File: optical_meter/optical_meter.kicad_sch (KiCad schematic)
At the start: 47 parts, among them J1 Conn_02x04, J2 SFP+, J3 Conn_01x02_Pin, U2 FIN1002M5X, U3 FIN1001M5X, U5 Pico

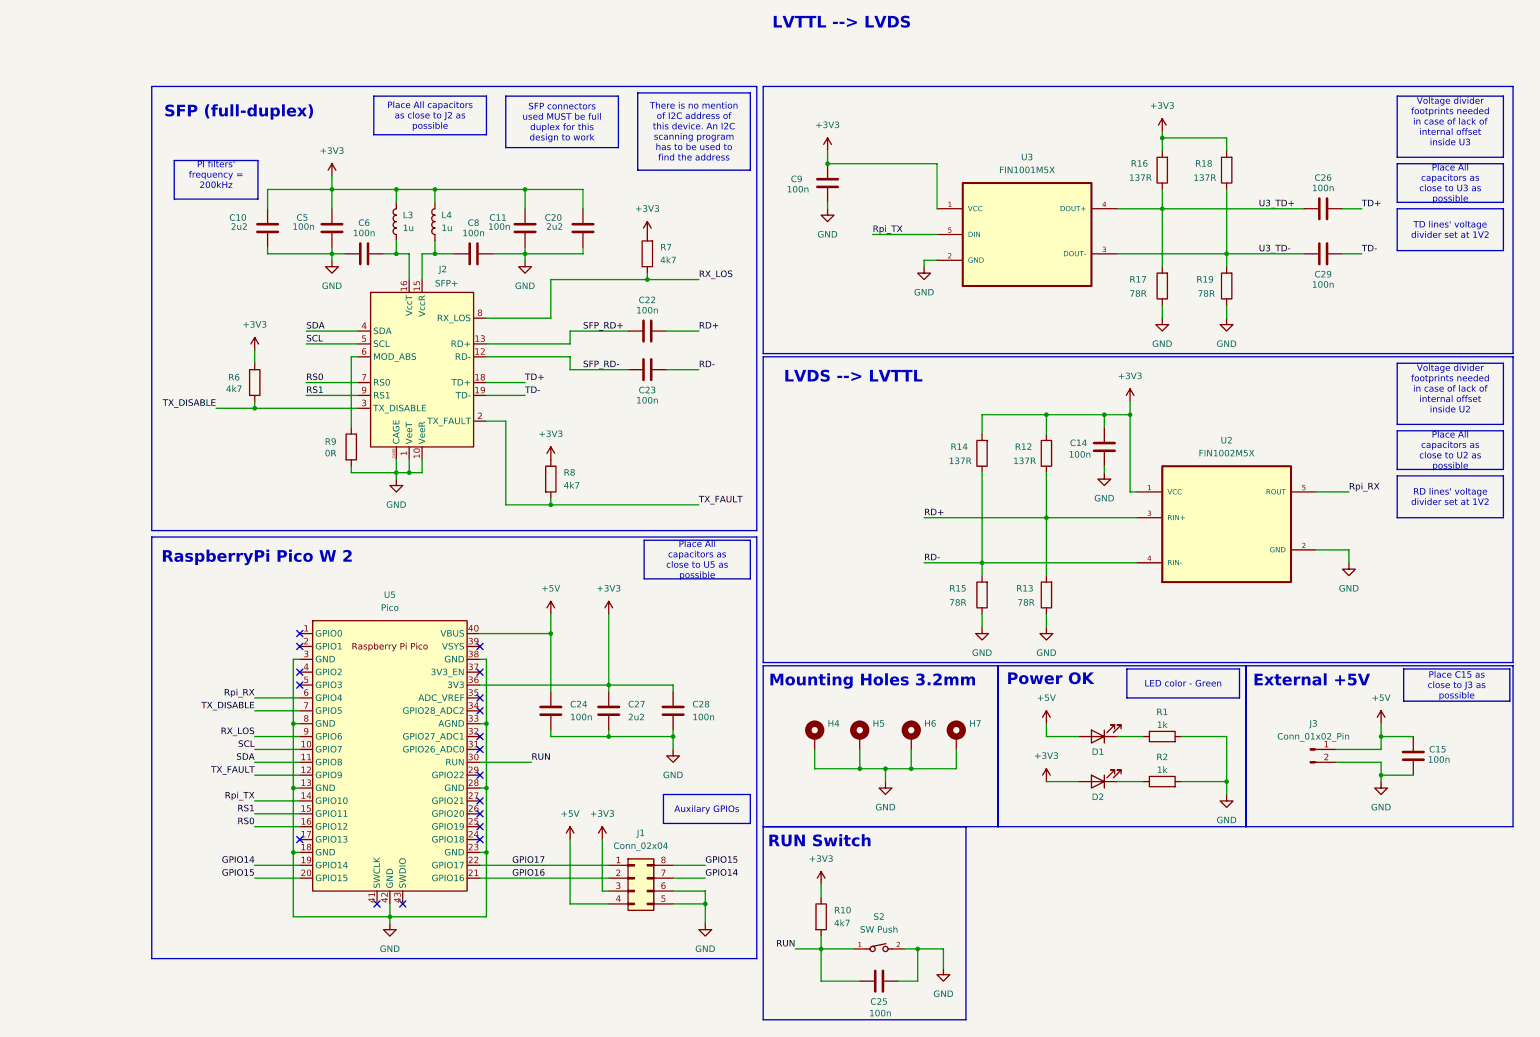
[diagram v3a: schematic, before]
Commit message: Finished layout. DRC passed except for courtyard and some footprint-schematic relaitions from KiCad that do not matter
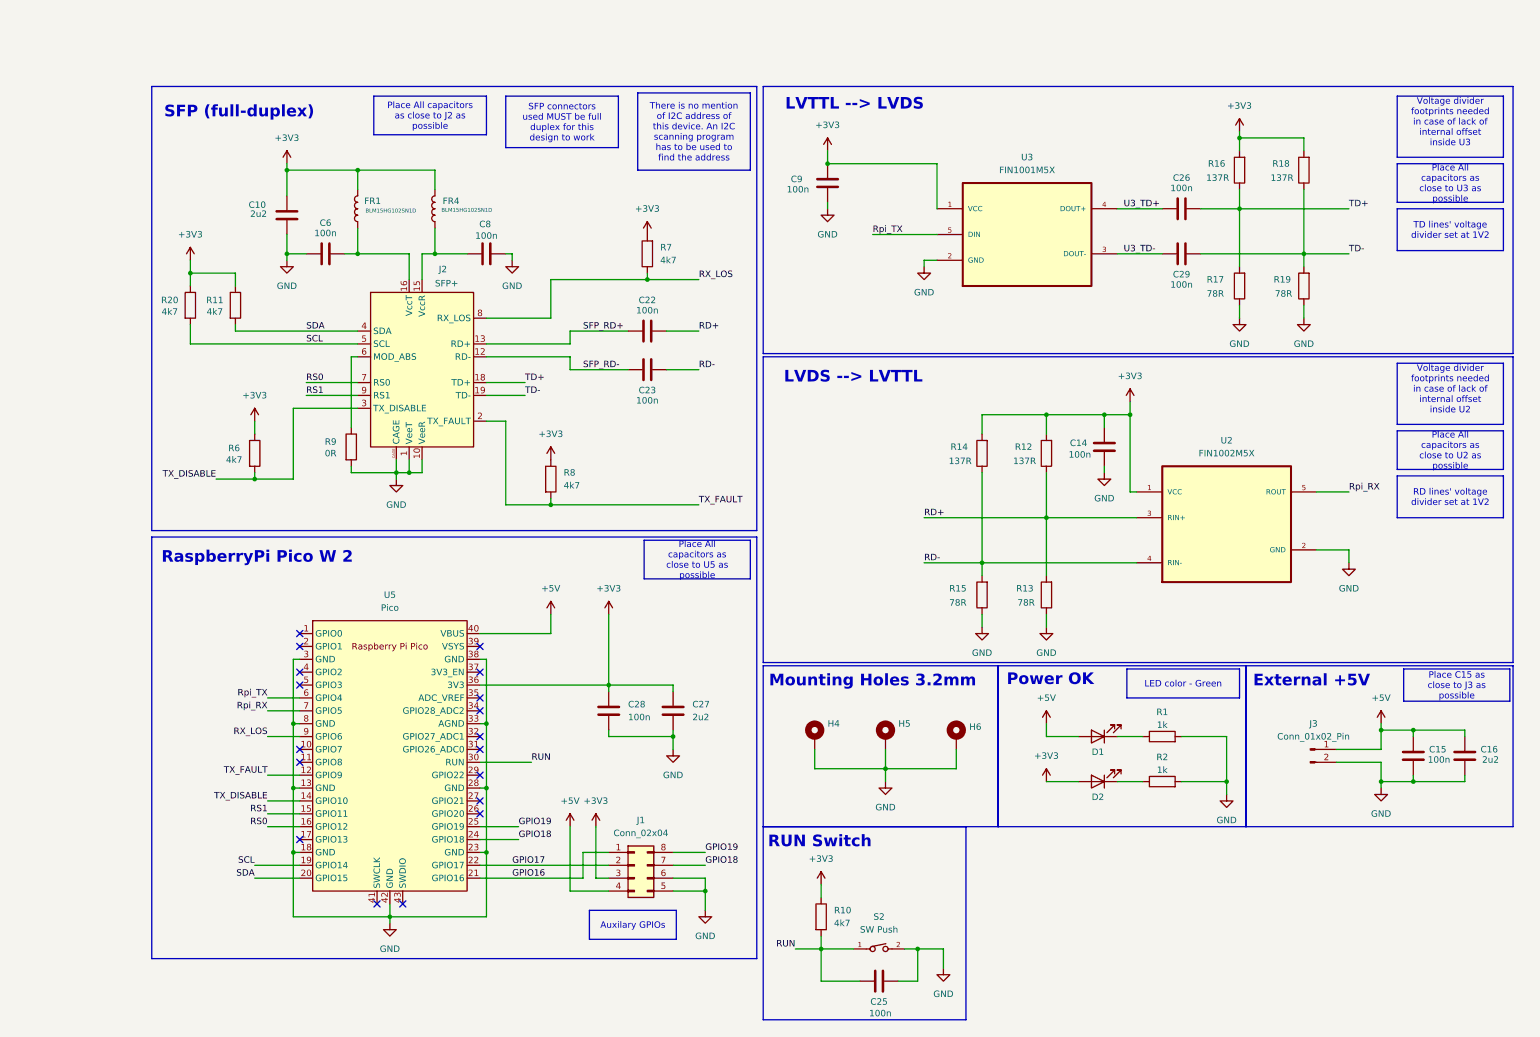
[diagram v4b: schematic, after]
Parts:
- removed C11, C24, C5: 100n, Capacitor_SMD:C_0603_1608Metric, symbol Device:C
- removed C20: 2u2, Capacitor_SMD:C_0603_1608Metric, symbol Device:C
- removed H6: ~, MountingHole:MountingHole_3.2mm_M3_DIN965_Pad, symbol Mechanical:MountingHole_Pad
- added C16: 2u2, Capacitor_SMD:C_0603_1608Metric, symbol Device:C
- added R11, R20: 4k7, Resistor_SMD:R_0603_1608Metric_Pad0.98x0.95mm_HandSolder, symbol Device:R
- D1, D2: footprint Diode_SMD:D_0603_1608Metric -> LED_SMD:LED_0603_1608Metric_Pad1.05x0.95mm_HandSolder
- FR1: renamed from L3; value 1u -> BLM15HG102SN1D; footprint Inductor_SMD:L_0805_2012Metric_Pad1.15x1.40mm_HandSolder -> Inductor_SMD:L_0402_1005Metric_Pad0.77x0.64mm_HandSolder
- FR4: renamed from L4; value 1u -> BLM15HG102SN1D; footprint Inductor_SMD:L_0805_2012Metric_Pad1.15x1.40mm_HandSolder -> Inductor_SMD:L_0402_1005Metric_Pad0.77x0.64mm_HandSolder
- renumbered H7 to H6
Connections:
- net +3V3: now also R11.1, R20.1
- net +5V: now also C16.1
- net GND: now also C16.2
- net GPIO16: now also J1.1 (Pin_1); no longer J1.2 (Pin_2)
- net GPIO17: now also J1.2 (Pin_2); no longer J1.1 (Pin_1)
- net Rpi_RX: now also U5.7 (GPIO5); no longer U5.6 (GPIO4)
- net Rpi_TX: now also U5.6 (GPIO4); no longer U5.14 (GPIO10)
- net SCL: now also U5.19 (GPIO14), R20.2; no longer U5.10 (GPIO7)
- net SDA: now also U5.20 (GPIO15), R11.2; no longer U5.11 (GPIO8)
- net TD+: now also R16.1, R17.2
- net TD-: now also R18.1, R19.2
- net TX_DISABLE: now also U5.14 (GPIO10); no longer U5.7 (GPIO5)
- net U3_TD+: no longer R16.1, R17.2
- net U3_TD-: no longer R18.1, R19.2
- net GPIO18: now reaches U5.24 (GPIO18)
- net GPIO18: now also J1.7 (Pin_7)
- net GPIO19: now reaches U5.25 (GPIO19)
- net GPIO19: now also J1.8 (Pin_8)
- removed net GPIO14: J1.7 (Pin_7), U5.19 (GPIO14)
- removed net GPIO15: J1.8 (Pin_8), U5.20 (GPIO15)
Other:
- moved on the sheet: C10, C26, C27, C28, C29, C6, C8, FR1, FR4, H5, J1, R16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

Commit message: changing the layout (in progress)
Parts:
- removed H5: ~, MountingHole:MountingHole_3.2mm_M3_DIN965_Pad, symbol Mechanical:MountingHole_Pad
- C10, C27: value 2u2 -> 4u7
- R2: value 1k -> 680R
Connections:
- net +3V3: now also J1.4 (Pin_4), R2.1; no longer D2.2 (A)
- net +5V: now also R1.1; no longer D1.2 (A), J1.4 (Pin_4)
- net GND: now also D1.1 (K), D2.1 (K); no longer R1.2, R2.2
- new net: D2.2 (A), R2.2
- new net: D1.2 (A), R1.2
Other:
- moved on the sheet: D1, D2, R1, R2
